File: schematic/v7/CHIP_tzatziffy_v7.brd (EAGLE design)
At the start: 40.9 x 49.8 mm, 57 parts, among them J1 2X20-CHIP0.7_DRILL, Q2 2N7002ET1G, U1 LMR62421, U3 DS2431P, X1 FH12-40S-0.5SH

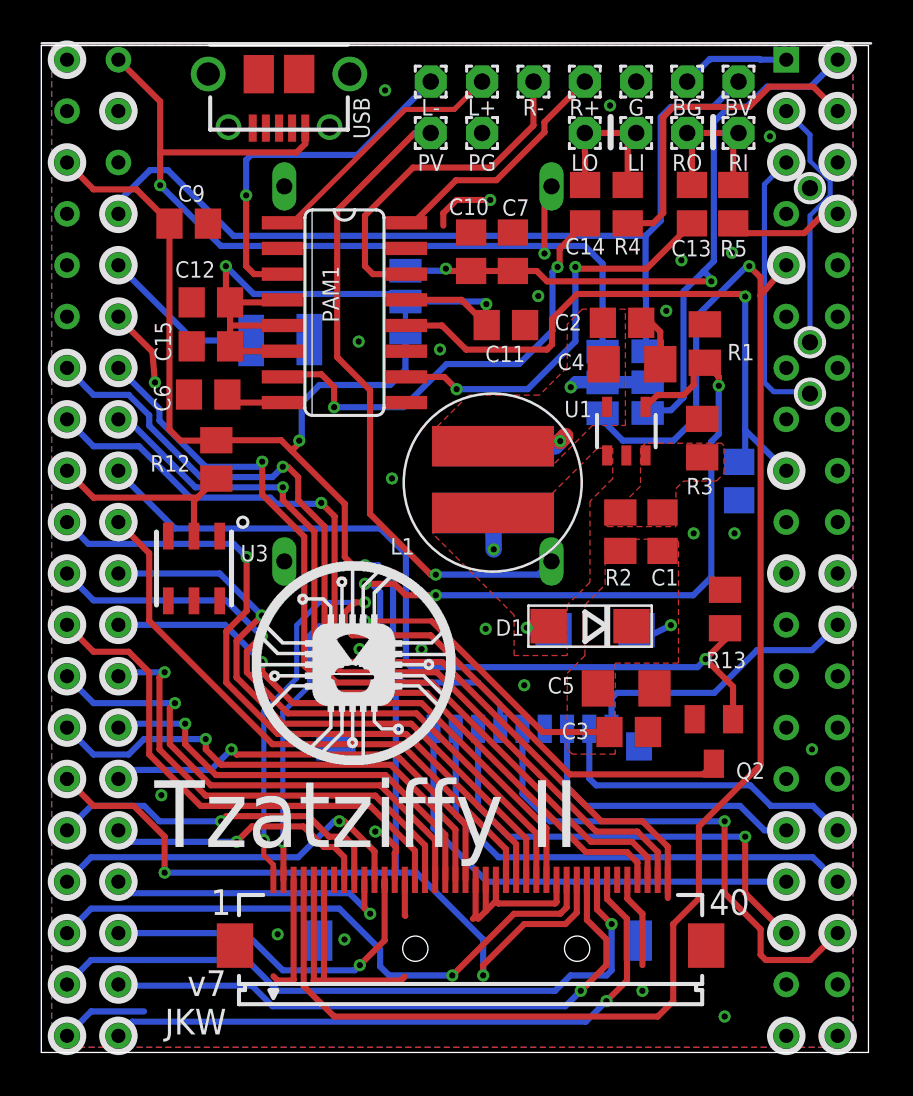
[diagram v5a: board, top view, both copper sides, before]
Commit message: added alternate dc/dc switch
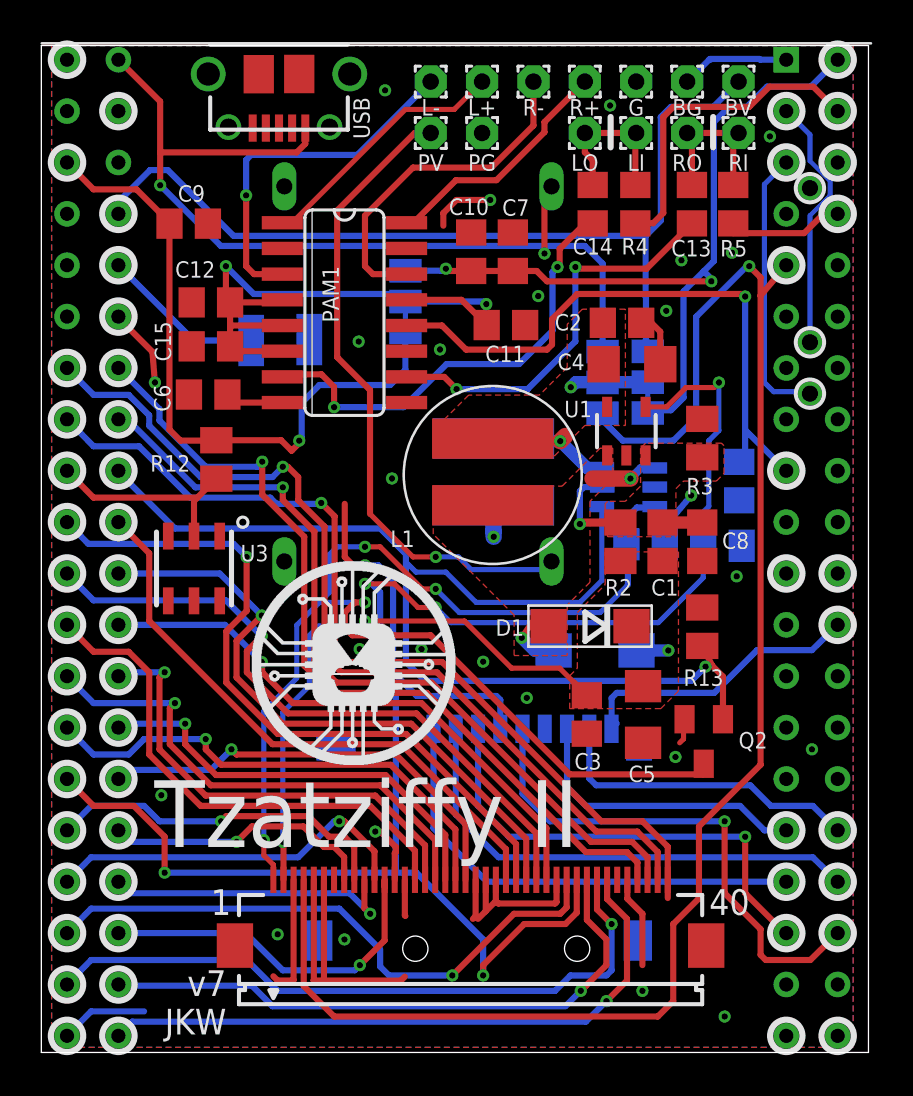
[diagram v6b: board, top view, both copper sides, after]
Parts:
- added C8: 10nF, rcl:C0805
- added R7: 5 / n.a., rcl:M0805
- added U$27: AP3032 / n.a., JKW_CHIP:SOT23-6
- Q2: value 2N7002ET1G -> n.a. / 2N7002ET1G
- R1: value 100K -> n.a. / 100k
- R13: value 10K -> n.a. / 10K
- R2: value 31.6k -> 0R / 31.6k
- R3: value 2.21k -> n.a./2.21k/4.53k
- SJ1: value (none) -> SMD_SJ_3WAY_CLOSED; device SparkFun-Retired:SJ_2 -> JKW_CHIP:SMD_SJ_3WAY_CLOSED
- SJ4: value SMD_SJ_3WAY_CLOSED -> (none); device JKW_CHIP:SMD_SJ_3WAY_CLOSED -> JKW_CHIP:SMD_SJ_3WAY_OPEN
- U1: value LMR62421 -> n.a. / LMR62421
- moved R1 10.0 mm to (33.7, 25.1), flipped to the bottom, turned to 180 degrees
- moved C3 2.25 mm to (27.0, 16.7), turned to 270 degrees
- moved C5 1.54 mm to (29.8, 16.7), turned to 270 degrees
- moved R13 1.43 mm to (32.7, 21.1)
- moved D2 1.00 mm to (27.4, 19.9)
- moved Q2 0.50 mm to (32.8, 15.4)
- moved C1 0.50 mm to (30.7, 25.2)
- moved R2 0.50 mm to (28.6, 25.2)
- moved L2 0.38 mm to (22.4, 28.6)
- moved C14 0.38 mm to (27.3, 41.9)
- moved L1 0.38 mm to (22.3, 28.6)
- moved R4 0.38 mm to (29.4, 41.9)
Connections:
- net DC_IN: now also U$27.6
- net DISPL_GND: now also R7.2, U$27.3
- net FB: now also C8.1, U$27.5
- net GND: now also C8.2, R7.1, U$27.2
- net PWM: now also U$27.4
- net VREG_OUTPUT: now also U$27.1
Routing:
- net DISPL_GND: track 40.7 -> 65.0 mm, vias 2 -> 4
- net PWM: track 42.1 -> 55.9 mm
- net FB: track 0.00 -> 6.81 mm, vias 0 -> 1
- net GND: track 59.4 -> 63.6 mm, vias 26 -> 27
- net VREG_OUTPUT: track 3.77 -> 7.59 mm, vias 2 -> 3
- net VCC3V3: track 55.3 -> 51.7 mm
- net DC_IN: track 8.02 -> 10.9 mm
- net PWR_LGT: track 32.0 -> 30.1 mm
- net AUDIO_L: track 16.6 -> 17.2 mm
